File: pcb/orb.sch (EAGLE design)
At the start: 6 parts

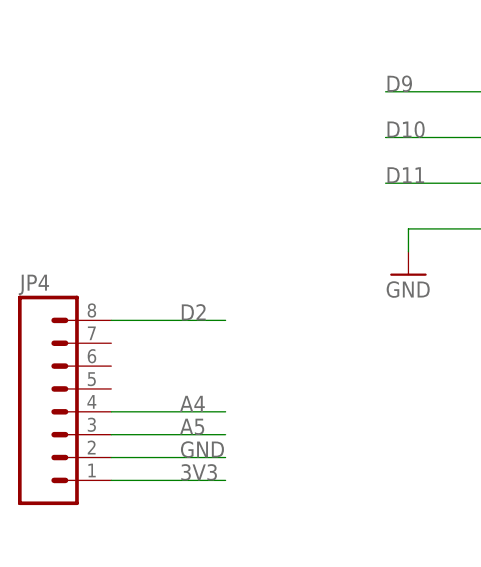
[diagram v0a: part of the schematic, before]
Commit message: changed name of component to reflect it's where the sensor goes
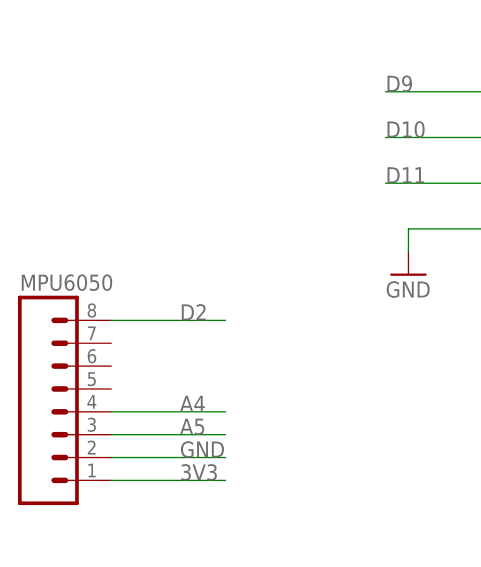
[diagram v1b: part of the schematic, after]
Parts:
- renumbered JP4 to MPU6050
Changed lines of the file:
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@@
 <part name="P+3" library="supply1" deviceset="VCC" device=""/>
 <part name="P+5" library="supply1" deviceset="VCC" device=""/>
-<part name="JP4" library="SparkFun-Connectors" deviceset="M08" device="1X08"/>
+<part name="MPU6050" library="SparkFun-Connectors" deviceset="M08" device="1X08"/>
 </parts>
 <sheets>
@@
 <instance part="P+3" gate="VCC" x="116.84" y="116.84" rot="R270"/>
 <instance part="P+5" gate="VCC" x="40.64" y="144.78" rot="R270"/>
-<instance part="JP4" gate="G$1" x="27.94" y="96.52"/>
+<instance part="MPU6050" gate="G$1" x="27.94" y="96.52"/>
 </instances>
 <busses>
@@
 </segment>
 <segment>
-<pinref part="JP4" gate="G$1" pin="2"/>
+<pinref part="MPU6050" gate="G$1" pin="2"/>
 <wire x1="33.02" y1="91.44" x2="45.72" y2="91.44" width="0.1524" layer="91"/>
 <label x="40.64" y="91.44" size="1.778" layer="95"/>
@@
 </segment>
 <segment>
-<pinref part="JP4" gate="G$1" pin="4"/>
+<pinref part="MPU6050" gate="G$1" pin="4"/>
 <wire x1="33.02" y1="96.52" x2="45.72" y2="96.52" width="0.1524" layer="91"/>
 <label x="40.64" y="96.52" size="1.778" layer="95"/>
@@
 </segment>
 <segment>
-<pinref part="JP4" gate="G$1" pin="3"/>
+<pinref part="MPU6050" gate="G$1" pin="3"/>
 <wire x1="33.02" y1="93.98" x2="45.72" y2="93.98" width="0.1524" layer="91"/>
 <label x="40.64" y="93.98" size="1.778" layer="95"/>
@@
 </segment>
 <segment>
-<pinref part="JP4" gate="G$1" pin="1"/>
+<pinref part="MPU6050" gate="G$1" pin="1"/>
 <wire x1="33.02" y1="88.9" x2="45.72" y2="88.9" width="0.1524" layer="91"/>
 <label x="40.64" y="88.9" size="1.778" layer="95"/>
@@
 </segment>
 <segment>
-<pinref part="JP4" gate="G$1" pin="8"/>
+<pinref part="MPU6050" gate="G$1" pin="8"/>
 <wire x1="33.02" y1="106.68" x2="45.72" y2="106.68" width="0.1524" layer="91"/>
 <label x="40.64" y="106.68" size="1.778" layer="95"/>
